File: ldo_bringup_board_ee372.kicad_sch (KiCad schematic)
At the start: 74 parts, among them J1 VIN, J10 MD_SW_EN, J13 VSIG, J14 VSIG_BUF, J15 NR, J18 VIN_PROBE, J19 VREF_PROBE, J2 GND, J20 VOUT_PROBE, J3 IBIAS, J4 VOUT, J5 VIN_SMA, J6 VOUT_SMA, J7 GND, J8 5V, Q1 FDV305N, Q2 FDV305N, Q3 FDV305N, Q4 FDV305N, Q5 FDV305N, SW1 MD_SW, U1 LDO_DualMode_BGR_EE372

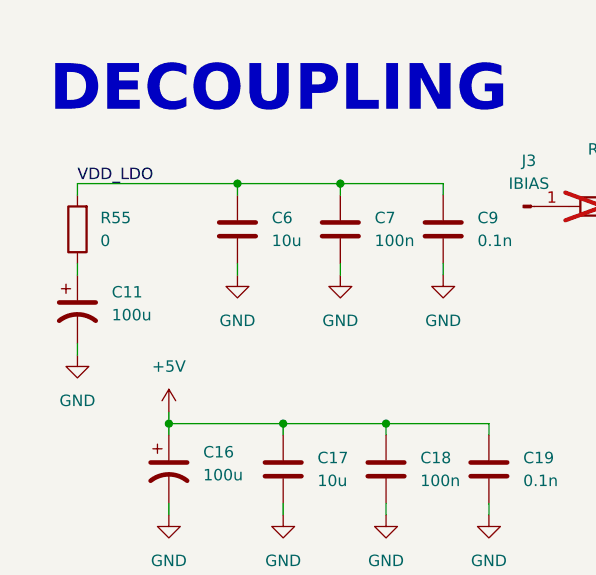
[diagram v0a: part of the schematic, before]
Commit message: Move C11 to VDD, remove R55, widen the analog tracks
Schematic: R55 removed. C11 pin 1 moves from VDD_LDO (through R55) to VDD,
the J1 side of R4. 151 parts, 109 nets, ERC 0 errors.

PCB:
- C11 moved to (114.5, 59.75), R55 footprint removed
- VOUT_LDO widened from 0.3 to 0.7 mm
- VSIG and VSIG_BUF widened from 0.3 to 0.6 mm, the R34 to R40 link and
  the R40 stub onto VDD_LDO to 0.7 mm
- J6 output and the noise amplifier input, outputs, stage links, supply
  and 2.5 V reference widened from 0.3 to 0.6 or 0.7 mm
- U3 sense tracks from R4 to R31 and R32 rerouted as a pair, R20 to R4
  links widened from 0.15 to 0.7 mm
- J12 moved to (126.25, 117.75), TP4 to (159.25, 83.0), R29 0.25 mm left
- VDD_LDO and +3V3 pour outlines on In2.Cu adjusted

DRC 0 errors, 0 unconnected, schematic parity 0.
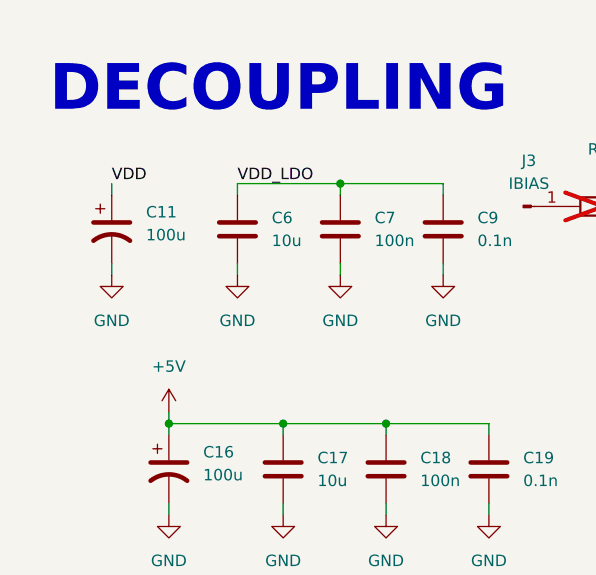
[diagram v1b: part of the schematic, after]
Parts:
- removed R55: 0, Resistor_SMD:R_0805_2012Metric_Pad1.20x1.40mm_HandSolder, symbol Device:R
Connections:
- net VDD: now also C11.1
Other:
- moved on the sheet: C11
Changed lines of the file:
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@@
 	)
 	(junction
-		(at 36.83 151.13)
-		(diameter 0)
-		(color 0 0 0 0)
-	)
-	(junction
 		(at 212.09 128.27)
 		(diameter 0)
@@
 	(wire
 		(pts
-			(xy 19.05 161.29) (xy 19.05 160.02)
+			(xy 22.86 152.4) (xy 22.86 151.13)
 		)
 		(stroke
@@
 	(wire
 		(pts
-			(xy 19.05 168.91) (xy 19.05 170.18)
+			(xy 22.86 160.02) (xy 22.86 161.29)
 		)
 		(stroke
@@
 	(wire
 		(pts
-			(xy 19.05 151.13) (xy 36.83 151.13)
-		)
-		(stroke
-			(width 0)
-			(type default)
-		)
-	)
-	(wire
-		(pts
-			(xy 19.05 151.13) (xy 19.05 152.4)
-		)
-		(stroke
-			(width 0)
-			(type default)
-		)
-	)
-	(wire
-		(pts
 			(xy 214.63 152.4) (xy 214.63 153.67)
 		)
@@
 	)
 	(label "VDD_LDO"
-		(at 19.05 151.13 0)
+		(at 36.83 151.13 0)
 		(effects
 			(font
@@
 		)
 	)
+	(label "VDD"
+		(at 22.86 151.13 0)
+		(effects
+			(font
+				(size 1.27 1.27)
+			)
+			(justify left bottom)
+		)
+	)
 	(label "VG3"
 		(at 237.49 142.24 0)
@@
 	(symbol
 		(lib_id "power:GND")
-		(at 19.05 170.18 0)
+		(at 22.86 161.29 0)
 		(unit 1)
 		(body_style 1)
@@
 		(fields_autoplaced yes)
 		(property "Reference" "#PWR011"
-			(at 19.05 176.53 0)
+			(at 22.86 167.64 0)
 			(hide yes)
 			(show_name no)
@@
 		)
 		(property "Value" "GND"
-			(at 19.05 175.26 0)
+			(at 22.86 166.37 0)
 			(show_name no)
 			(do_not_autoplace no)
@@
 		)
 		(property "Footprint" ""
-			(at 19.05 170.18 0)
+			(at 22.86 161.29 0)
 			(hide yes)
 			(show_name no)
@@
 		)
 		(property "Datasheet" ""
-			(at 19.05 170.18 0)
+			(at 22.86 161.29 0)
 			(hide yes)
 			(show_name no)
@@
 		)
 		(property "Description" "Power symbol creates a global label with name \"GND\" , ground"
-			(at 19.05 170.18 0)
+			(at 22.86 161.29 0)
 			(hide yes)
 			(show_name no)
@@
 	(symbol
 		(lib_id "Device:C_Polarized_US")
-		(at 19.05 165.1 0)
+		(at 22.86 156.21 0)
 		(unit 1)
 		(body_style 1)
@@
 		(fields_autoplaced yes)
 		(property "Reference" "C11"
-			(at 22.86 163.1949 0)
+			(at 26.67 154.3049 0)
 			(show_name no)
 			(do_not_autoplace no)
@@
 		)
 		(property "Value" "100u"
-			(at 22.86 165.7349 0)
+			(at 26.67 156.8449 0)
 			(show_name no)
 			(do_not_autoplace no)
@@
 		)
 		(property "Footprint" "Capacitor_THT:CP_Radial_D6.3mm_P2.50mm"
-			(at 19.05 165.1 0)
+			(at 22.86 156.21 0)
 			(hide yes)
 			(show_name no)
@@
 		)
 		(property "Datasheet" "https://industrial.panasonic.com/cdbs/www-data/pdf/RDF0000/ABA0000C1209.pdf"
-			(at 19.05 165.1 0)
+			(at 22.86 156.21 0)
 			(hide yes)
 			(show_name no)
@@
 		)
 		(property "Description" "CAP ALUM 100UF 20% 25V RADIAL TH"
-			(at 19.05 165.1 0)
+			(at 22.86 156.21 0)
 			(hide yes)
 			(show_name no)
@@
 		)
 		(property "Manufacturer" "Panasonic Industry"
-			(at 19.05 165.1 0)
+			(at 22.86 156.21 0)
 			(hide yes)
 			(show_name no)
@@
 		)
 		(property "Manufacturer Part Number" "EEU-FC1E101S"
-			(at 19.05 165.1 0)
+			(at 22.86 156.21 0)
 			(hide yes)
 			(show_name no)
@@
 		)
 		(property "Distributer Link 1" "https://www.digikey.com/en/products/detail/panasonic-electronic-components/EEU-FC1E101S/266278"
-			(at 19.05 165.1 0)
+			(at 22.86 156.21 0)
 			(hide yes)
 			(show_name no)
@@
 					(unit 1)
 				)
-			)
-		)
-	)
-	(symbol
-		(lib_id "Device:R")
-		(at 19.05 156.21 180)
-		(unit 1)
-		(body_style 1)
-		(exclude_from_sim no)
-		(in_bom yes)
-		(on_board yes)
-		(in_pos_files yes)
-		(dnp no)
-		(fields_autoplaced yes)
-		(property "Reference" "R55"
-			(at 21.59 154.9399 0)
-			(show_name no)
-			(do_not_autoplace no)
-			(effects
-				(font
-					(size 1.27 1.27)
-				)
-				(justify right)
-			)
-		)
-		(property "Value" "0"
-			(at 21.59 157.4799 0)
-			(show_name no)
-			(do_not_autoplace no)
-			(effects
-				(font
-					(size 1.27 1.27)
-				)
-				(justify right)
-			)
-		)
-		(property "Footprint" "Resistor_SMD:R_0805_2012Metric_Pad1.20x1.40mm_HandSolder"
-			(at 20.828 156.21 90)
-			(hide yes)
-			(show_name no)
-			(do_not_autoplace no)
-			(effects
-				(font
-					(size 1.27 1.27)
-				)
-			)
-		)
-		(property "Datasheet" "https://www.vishay.com/docs/20043/crcwhpe3.pdf"
-			(at 19.05 156.21 0)
-			(hide yes)
-			(show_name no)
-			(do_not_autoplace no)
-			(effects
-				(font
-					(size 1.27 1.27)
-				)
-			)
-		)
-		(property "Description" "0 ohm jumper, 0805, 6 A max"
-			(at 19.05 156.21 0)
-			(hide yes)
-			(show_name no)
-			(do_not_autoplace no)
-			(effects
-				(font
-					(size 1.27 1.27)
-				)
-			)
-		)
-		(property "Manufacturer" "Vishay Dale"
-			(at 19.05 156.21 0)
-			(hide yes)
-			(show_name no)
-			(do_not_autoplace no)
-			(effects
-				(font
-					(size 1.27 1.27)
-				)
-			)
-		)
-		(property "Manufacturer Part Number" "CRCW08050000Z0EAHP"
-			(at 19.05 156.21 0)
-			(hide yes)
-			(show_name no)
-			(do_not_autoplace no)
-			(effects
-				(font
-					(size 1.27 1.27)
-				)
-			)
-		)
-		(property "Distributer Link 1" "https://www.digikey.com/en/products/detail/vishay-dale/CRCW08050000Z0EAHP/2222316"
-			(at 19.05 156.21 0)
-			(hide yes)
-			(show_name no)
-			(do_not_autoplace no)
-			(effects
-				(font
-					(size 1.27 1.27)
-				)
-			)
-		)
-		(pin "2"
-		)
-		(pin "1"
-		)
-		(instances
-			(project "ldo_bringup_board_ee372"
-				(path "/d41ff68c-d87d-4b82-b500-4ee675d17cf6"
-					(reference "R55")
-					(unit 1)
-				)

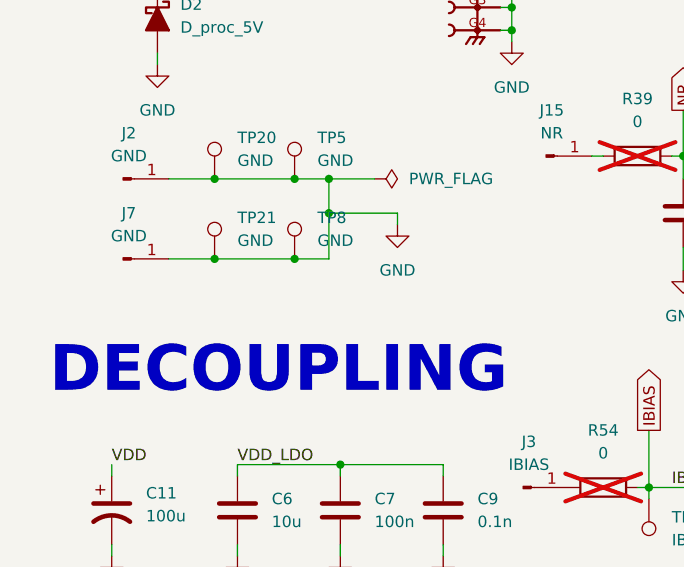
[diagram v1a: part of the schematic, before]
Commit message: Add seven ground test points, TP22 to TP25 and TP31 to TP33
Keystone 5006 on GND in the schematic, footprints added to the PCB and
parked outside the board outline. Not placed yet, so DRC shows them
unconnected.
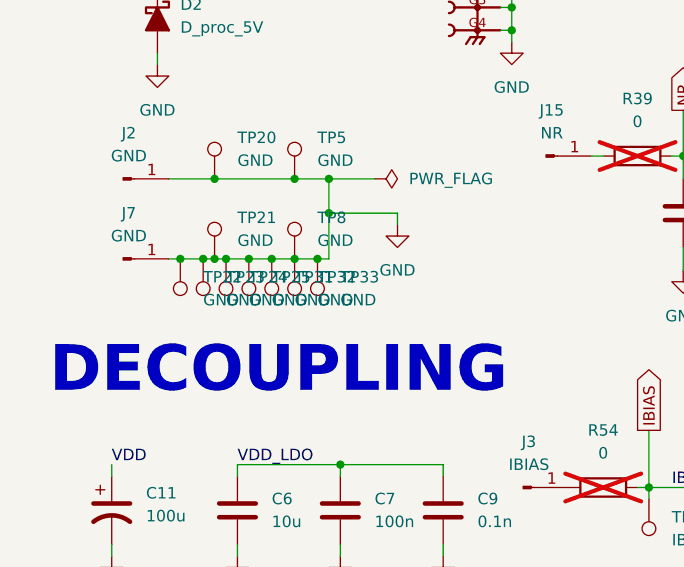
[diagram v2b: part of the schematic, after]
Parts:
- added TP22, TP23, TP24, TP25, TP31, TP32, TP33: GND, TestPoint:TestPoint_Keystone_5005-5009_Compact, symbol Connector:TestPoint
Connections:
- net GND: now also TP22.1, TP23.1, TP24.1, TP25.1, TP31.1, TP32.1, TP33.1

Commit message: Add three spare through-hole pads, TP35 to TP37
Keystone test point footprints valued SP1, SP2 and SP3, marked DNP and
left unconnected, placed along the top edge at y = 55.5. GND stitching
vias near them moved, four added and one removed.

161 parts, 112 nets. DRC 0 errors, 0 unconnected, schematic parity 0.
ERC 0 errors.
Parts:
- added TP35: SP1, TestPoint:TestPoint_Keystone_5005-5009_Compact, symbol Connector:TestPoint
- added TP36: SP2, TestPoint:TestPoint_Keystone_5005-5009_Compact, symbol Connector:TestPoint
- added TP37: SP3, TestPoint:TestPoint_Keystone_5005-5009_Compact, symbol Connector:TestPoint
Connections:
- no-connect marks 0 -> 3

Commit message: Add a Pin Defaults sheet with the MD pin table
New hierarchical sheet pin_defaults.kicad_sch, text only. It states how
the MD pin (pin 29) is set by SW1 through R2 with J10 fitted, or by the
Teensy through Q6 with J9 and J11 fitted, and that HI is high power mode
and LO is low power mode.

No parts or nets change. PCB unchanged. ERC 0 errors, DRC 0 errors,
schematic parity 0.
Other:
- added sheet Pin Defaults (pin_defaults.kicad_sch)
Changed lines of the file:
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@@
+	)
+	(sheet
+		(at 116.84 20.955)
+		(size 12.7 5.08)
+		(exclude_from_sim no)
+		(in_bom yes)
+		(on_board yes)
+		(dnp no)
+		(fields_autoplaced yes)
+		(stroke
+			(width 0.1524)
+			(type solid)
+		)
+		(fill
+			(color 0 0 0 0)
+		)
+		(property "Sheetname" "Pin Defaults"
+			(at 116.84 20.2434 0)
+			(show_name no)
+			(do_not_autoplace no)
+			(effects
+				(font
+					(size 1.27 1.27)
+				)
+				(justify left bottom)
+			)
+		)
+		(property "Sheetfile" "pin_defaults.kicad_sch"
+			(at 116.84 26.6196 0)
+			(show_name no)
+			(do_not_autoplace no)
+			(effects
+				(font
+					(size 1.27 1.27)
+				)
+				(justify left top)
+			)
+		)
+		(instances
+			(project "ldo_bringup_board_ee372"
+				(path "/d41ff68c-d87d-4b82-b500-4ee675d17cf6"
+					(page "6")
+				)
+			)
+		)
 	)
 	(sheet

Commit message: Add R55, a 0 ohm link between VOUT_LDO and a new VNOISE net
Schematic: R55 (0 ohm 0805, fitted) has pin 2 on VOUT_LDO and pin 1 on a
new net, VNOISE. C10 pin 1 (the J6 SMA coupling cap) and R44 pin 1 (the
noise amplifier input link) move from VOUT_LDO to VNOISE.
162 parts, 113 nets, ERC 0 errors.

PCB: R55 placed at (191.625, 88.775). The old VOUT_LDO tracks to C10 and
R44 are rerouted as VNOISE, 35.6 mm at 0.7 mm, 27 mm of it on B.Cu
through two new vias. Seven GND vias added along x = 164.5.
DRC 0 errors, 0 unconnected, schematic parity 0.

The exported Gerber, drill, CPL and report files in the repo predate
this change.
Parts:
- added R55: 0, Resistor_SMD:R_0805_2012Metric_Pad1.20x1.40mm_HandSolder, symbol Device:R
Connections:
- net SHUNT_OUT_A: now also R55.2; no longer C10.1
- new net VNOISE: C10.1, R55.1
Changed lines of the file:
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@@
 	(wire
 		(pts
+			(xy 227.33 43.18) (xy 227.33 39.37)
+		)
+		(stroke
+			(width 0)
+			(type default)
+		)
+	)
+	(wire
+		(pts
 			(xy 29.21 176.53) (xy 29.21 177.8)
 		)
@@
 	(wire
 		(pts
-			(xy 227.33 54.61) (xy 227.33 39.37)
+			(xy 227.33 54.61) (xy 227.33 50.8)
 		)
 		(stroke
@@
 					(unit 1)
 				)
+			)
+		)
+	)
+	(symbol
+		(lib_id "Device:R")
+		(at 227.33 46.99 180)
+		(unit 1)
+		(body_style 1)
+		(exclude_from_sim no)
+		(in_bom yes)
+		(on_board yes)
+		(in_pos_files yes)
+		(dnp no)
+		(fields_autoplaced yes)
+		(property "Reference" "R55"
+			(at 229.87 45.7199 0)
+			(show_name no)
+			(do_not_autoplace no)
+			(effects
+				(font
+					(size 1.27 1.27)
+				)
+				(justify right)
+			)
+		)
+		(property "Value" "0"
+			(at 229.87 48.2599 0)
+			(show_name no)
+			(do_not_autoplace no)
+			(effects
+				(font
+					(size 1.27 1.27)
+				)
+				(justify right)
+			)
+		)
+		(property "Footprint" "Resistor_SMD:R_0805_2012Metric_Pad1.20x1.40mm_HandSolder"
+			(at 229.108 46.99 90)
+			(hide yes)
+			(show_name no)
+			(do_not_autoplace no)
+			(effects
+				(font
+					(size 1.27 1.27)
+				)
+			)
+		)
+		(property "Datasheet" "https://www.vishay.com/docs/20043/crcwhpe3.pdf"
+			(at 227.33 46.99 0)
+			(hide yes)
+			(show_name no)
+			(do_not_autoplace no)
+			(effects
+				(font
+					(size 1.27 1.27)
+				)
+			)
+		)
+		(property "Description" "0 ohm jumper, 0805, 6 A max"
+			(at 227.33 46.99 0)
+			(hide yes)
+			(show_name no)
+			(do_not_autoplace no)
+			(effects
+				(font
+					(size 1.27 1.27)
+				)
+			)
+		)
+		(property "Manufacturer" "Vishay Dale"
+			(at 227.33 46.99 0)
+			(hide yes)
+			(show_name no)
+			(do_not_autoplace no)
+			(effects
+				(font
+					(size 1.27 1.27)
+				)
+			)
+		)
+		(property "Manufacturer Part Number" "CRCW08050000Z0EAHP"
+			(at 227.33 46.99 0)
+			(hide yes)
+			(show_name no)
+			(do_not_autoplace no)
+			(effects
+				(font
+					(size 1.27 1.27)
+				)
+			)
+		)
+		(property "Distributer Link 1" "https://www.digikey.com/en/products/detail/vishay-dale/CRCW08050000Z0EAHP/2222316"
+			(at 227.33 46.99 0)
+			(hide yes)
+			(show_name no)
+			(do_not_autoplace no)
+			(effects
+				(font
+					(size 1.27 1.27)
+				)
+			)
+		)
+		(pin "2"
+		)
+		(pin "1"
+		)
+		(instances
+			(project "ldo_bringup_board_ee372"
+				(path "/d41ff68c-d87d-4b82-b500-4ee675d17cf6"
+					(reference "R55")
+					(unit 1)
+				)

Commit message: Add bring-up notes to the schematic
Text notes only, no parts or nets change. Leave R3, R21, R29 to R32,
R40, R44 and R55 off at first. Possibly lift C6 and C11 when driving
VIN from the buffer. Add a large pull-down on the buffer input.
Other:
- note added: "Add large pulldown so buffer input is not floating"
- note added: "Initially leave off R21"
- note added: "Initially leave off R3"
- note added: "Initially leave off R55"
- note added: "Potentially remove C11 and C6 when using buffer"
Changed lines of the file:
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@@
+		)
+	)
+	(text "Potentially remove C11 and C6 \nwhen using buffer"
+		(exclude_from_sim yes)
+		(at 35.052 171.45 0)
+		(effects
+			(font
+				(size 1.27 1.27)
+			)
+			(justify left)
+		)
+	)
+	(text "Initially leave off R3"
+		(exclude_from_sim yes)
+		(at 246.38 32.004 0)
+		(effects
+			(font
+				(size 1.27 1.27)
+			)
+			(justify left)
 		)
 	)
@@
 				(size 1.27 1.27)
 			)
+		)
+	)
+	(text "Add large pulldown \nso buffer input is \nnot floating"
+		(exclude_from_sim yes)
+		(at 70.358 99.822 0)
+		(effects
+			(font
+				(size 1.27 1.27)
+			)
+			(justify left)
+		)
+	)
+	(text "Initially leave off R55\n"
+		(exclude_from_sim yes)
+		(at 203.2 46.736 0)
+		(effects
+			(font
+				(size 1.27 1.27)
+			)
+			(justify left)
 		)
 	)
@@
 		)
 	)
+	(text "Initially leave off R21"
+		(exclude_from_sim yes)
+		(at 156.464 100.584 0)
+		(effects
+			(font
+				(size 1.27 1.27)
+			)
+			(justify left)
+		)
+	)
